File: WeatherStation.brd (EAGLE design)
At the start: 30.5 x 44.5 mm, 11 parts, among them J1 EDISON_CONNECTOR_FULLMOUNTING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, J2 EDISON_CONNECTOR_FULLHEADER

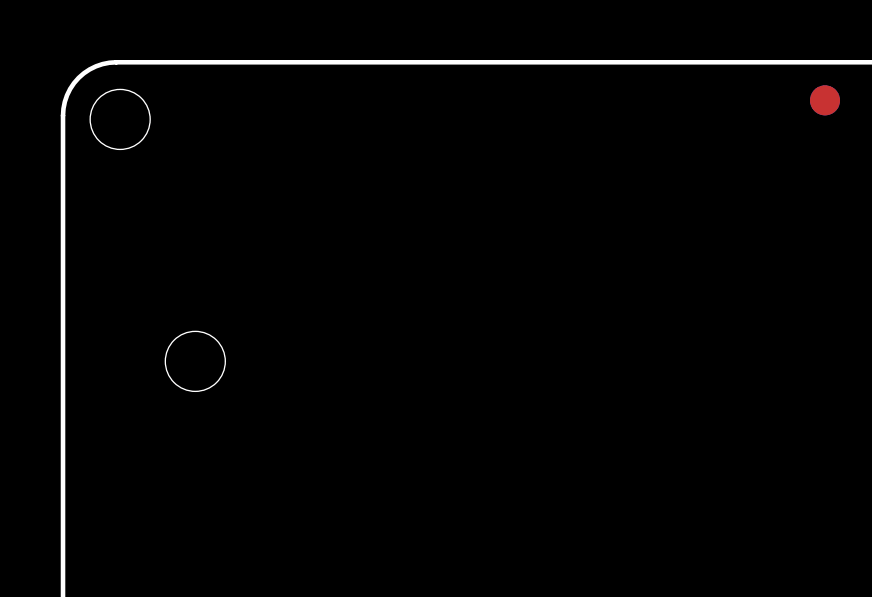
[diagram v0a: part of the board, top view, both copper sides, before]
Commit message: added MCP73831 circuit
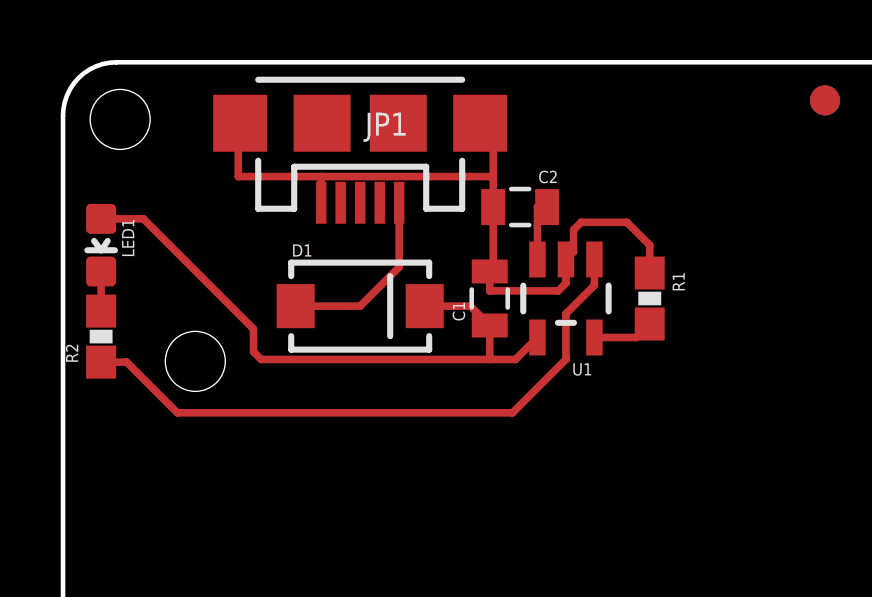
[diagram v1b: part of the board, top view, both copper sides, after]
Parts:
- added C1, C2: 4.7µF, SparkFun-Capacitors:0805
- added D1: MBRA140, SparkFun-DiscreteSemi:SMA-DIODE
- added JP1: USB-MICROB, SparkFun-Connectors:USB-MICROB
- added LED1: (no value), SparkFun-LED:LED-0603
- added R1: 2kΩ, SparkFun-Resistors:0603-RES
- added R2: 330Ω, SparkFun-Resistors:0603-RES
- added U1: MCP73831, SparkFun-PowerIC:SOT23-5
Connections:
- new net N$1: D1.A, JP1.VBUS
- new net N$2: C1.1, D1.C, LED1.A, U1.4
- new net N$4: LED1.C, R2.2
- new net N$5: R2.1, U1.1
- new net N$6: R1.2, U1.5
- new net VBAT: C2.1, U1.3
- net GND: now also C1.2, C2.2, JP1.GND, JP1.MT1, JP1.MT2, R1.1, U1.2
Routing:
- net GND: track 0.01 -> 25.7 mm
- net N$2: track 0.00 -> 20.8 mm
- net N$5: track 0.00 -> 20.7 mm
- net N$1: track 0.00 -> 6.13 mm
- net VBAT: track 0.00 -> 2.07 mm
- net N$6: track 0.00 -> 2.03 mm
- net N$4: track 0.00 -> 1.32 mm
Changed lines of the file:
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@@
 <?xml version="1.0" encoding="utf-8"?>
 <!DOCTYPE eagle SYSTEM "eagle.dtd">
-<eagle version="6.5.0">
+<eagle version="7.1.0">
 <drawing>
 <settings>
@@
 <pass name="Default">
 <param name="RoutingGrid" value="50mil"/>
+<param name="AutoGrid" value="1"/>
+<param name="Efforts" value="0"/>
+<param name="TopRouterVariant" value="1"/>
 <param name="tpViaShape" value="round"/>
 <param name="PrefDir.1" value="|"/>
@@
 <element name="FID3" library="SparkFun-Aesthetics" package="FIDUCIAL-1X2" value="FIDUCIAL1X2" x="1.27" y="5.08" locked="yes" rot="MR0"/>
 <element name="FID4" library="SparkFun-Aesthetics" package="FIDUCIAL-1X2" value="FIDUCIAL1X2" x="25.4" y="43.18" locked="yes" rot="MR0"/>
+<element name="JP1" library="SparkFun-Connectors" package="USB-MICROB" value="USB-MICROB" x="9.906" y="42.418" rot="R180">
+<attribute name="PROD_ID" value="CONN-09505" x="9.906" y="42.418" size="1.778" layer="27" rot="R180" display="off"/>
+</element>
+<element name="D1" library="SparkFun-DiscreteSemi" package="SMA-DIODE" value="MBRA140" x="9.906" y="36.322">
+<attribute name="PROD_ID" value="DIO-08053" x="9.906" y="36.322" size="1.778" layer="27" display="off"/>
+</element>
+<element name="U1" library="SparkFun-PowerIC" package="SOT23-5" value="MCP73831" x="16.764" y="36.576" smashed="yes" rot="R180">
+<attribute name="PROD_ID" value="IC-09995" x="16.764" y="36.576" size="1.778" layer="27" rot="R180" display="off"/>
+<attribute name="NAME" x="17.653" y="34.417" size="0.4064" layer="25" rot="R180"/>
+<attribute name="VALUE" x="16.7005" y="36.5125" size="0.3048" layer="27" rot="R180" align="center"/>
+</element>
+<element name="C1" library="SparkFun-Capacitors" package="0805" value="4.7µF" x="14.224" y="36.576" smashed="yes" rot="R90">
+<attribute name="NAME" x="13.3985" y="35.814" size="0.4064" layer="25" rot="R90"/>
+</element>
+<element name="R1" library="SparkFun-Resistors" package="0603-RES" value="2kΩ" x="19.558" y="36.576" rot="R270"/>
+<element name="C2" library="SparkFun-Capacitors" package="0805" value="4.7µF" x="15.24" y="39.624" smashed="yes" rot="R180">
+<attribute name="NAME" x="16.51" y="40.8305" size="0.4064" layer="25" rot="R180"/>
+</element>
+<element name="LED1" library="SparkFun-LED" package="LED-0603" value="" x="1.27" y="38.354" rot="R180"/>
+<element name="R2" library="SparkFun-Resistors" package="0603-RES" value="330Ω" x="1.27" y="35.306" rot="R90"/>
 </elements>
 <signals>
@@
 <wire x1="26.9438" y1="22.1798" x2="26.9494" y2="22.1742" width="0.1524" layer="1"/>
 <via x="27.1272" y="20.5232" extent="1-16" drill="0.3302"/>
+<contactref element="C1" pad="2"/>
+<contactref element="JP1" pad="MT2"/>
+<contactref element="JP1" pad="GND"/>
+<contactref element="JP1" pad="MT1"/>
+<contactref element="C2" pad="2"/>
+<contactref element="R1" pad="1"/>
+<contactref element="U1" pad="2"/>
+<wire x1="14.34" y1="39.624" x2="14.34" y2="40.64" width="0.254" layer="1"/>
+<wire x1="14.34" y1="40.64" x2="14.34" y2="42.418" width="0.254" layer="1"/>
+<wire x1="14.34" y1="42.418" x2="13.906" y2="42.418" width="0.254" layer="1"/>
+<wire x1="8.606" y1="39.768" x2="8.606" y2="40.64" width="0.254" layer="1"/>
+<wire x1="8.606" y1="40.64" x2="14.34" y2="40.64" width="0.254" layer="1"/>
+<wire x1="8.606" y1="40.64" x2="5.842" y2="40.64" width="0.254" layer="1"/>
+<wire x1="5.842" y1="40.64" x2="5.842" y2="42.418" width="0.254" layer="1"/>
+<wire x1="5.842" y1="42.418" x2="5.906" y2="42.418" width="0.254" layer="1"/>
+<wire x1="14.224" y1="37.476" x2="14.34" y2="37.592" width="0.254" layer="1"/>
+<wire x1="14.34" y1="37.592" x2="14.34" y2="39.624" width="0.254" layer="1"/>
+<wire x1="16.764" y1="37.8761" x2="16.764" y2="37.084" width="0.254" layer="1"/>
+<wire x1="16.764" y1="37.084" x2="16.51" y2="36.83" width="0.254" layer="1"/>
+<wire x1="16.51" y1="36.83" x2="14.224" y2="36.83" width="0.254" layer="1"/>
+<wire x1="14.224" y1="36.83" x2="14.224" y2="37.476" width="0.254" layer="1"/>
+<wire x1="19.558" y1="37.426" x2="19.558" y2="38.354" width="0.254" layer="1"/>
+<wire x1="19.558" y1="38.354" x2="18.796" y2="39.116" width="0.254" layer="1"/>
+<wire x1="18.796" y1="39.116" x2="17.272" y2="39.116" width="0.254" layer="1"/>
+<wire x1="17.272" y1="39.116" x2="17.018" y2="38.862" width="0.254" layer="1"/>
+<wire x1="17.018" y1="38.862" x2="17.018" y2="38.1301" width="0.254" layer="1"/>
+<wire x1="17.018" y1="38.1301" x2="16.764" y2="37.8761" width="0.254" layer="1"/>
+<wire x1="26.9438" y1="22.1798" x2="28.2448" y2="22.1742" width="0" layer="19" extent="1-1"/>
+<wire x1="25.96" y1="22.18" x2="26.9438" y2="22.1798" width="0" layer="19" extent="1-16"/>
+<wire x1="25.96" y1="22.1798" x2="25.96" y2="22.18" width="0" layer="19" extent="1-16"/>
+<wire x1="25.96" y1="22.98" x2="25.96" y2="22.18" width="0" layer="19" extent="16-16"/>
+<wire x1="25.96" y1="22.9798" x2="25.96" y2="22.98" width="0" layer="19" extent="1-16"/>
+<wire x1="25.96" y1="21.38" x2="25.96" y2="22.18" width="0" layer="19" extent="16-16"/>
+<wire x1="25.96" y1="21.3798" x2="25.96" y2="21.38" width="0" layer="19" extent="1-16"/>
+<wire x1="25.96" y1="20.98" x2="25.96" y2="21.38" width="0" layer="19" extent="16-16"/>
+<wire x1="25.96" y1="20.9798" x2="25.96" y2="20.98" width="0" layer="19" extent="1-16"/>
+<wire x1="25.96" y1="20.58" x2="25.96" y2="20.98" width="0" layer="19" extent="16-16"/>
+<wire x1="25.96" y1="20.5798" x2="25.96" y2="20.58" width="0" layer="19" extent="1-16"/>
+<wire x1="25.96" y1="20.18" x2="25.96" y2="20.58" width="0" layer="19" extent="16-16"/>
+<wire x1="25.96" y1="20.1798" x2="25.96" y2="20.18" width="0" layer="19" extent="1-16"/>
+<wire x1="27.1272" y1="20.5232" x2="25.96" y2="20.58" width="0" layer="19" extent="16-16"/>
+<wire x1="19.558" y1="37.426" x2="25.96" y2="22.98" width="0" layer="19" extent="1-16"/>
 </signal>
 <signal name="VSYS">
@@
 <wire x1="21.7988" y1="20.58" x2="21.799" y2="20.5798" width="0.1524" layer="1"/>
 </signal>
+<signal name="N$1">
+<contactref element="JP1" pad="VBUS"/>
+<contactref element="D1" pad="A"/>
+<wire x1="11.206" y1="39.768" x2="11.206" y2="37.622" width="0.254" layer="1"/>
+<wire x1="11.206" y1="37.622" x2="9.906" y2="36.322" width="0.254" layer="1"/>
+<wire x1="9.906" y1="36.322" x2="7.756" y2="36.322" width="0.254" layer="1"/>
+</signal>
+<signal name="N$2">
+<contactref element="D1" pad="C"/>
+<contactref element="U1" pad="4"/>
+<contactref element="C1" pad="1"/>
+<contactref element="LED1" pad="A"/>
+<wire x1="12.056" y1="36.322" x2="13.578" y2="36.322" width="0.254" layer="1"/>
+<wire x1="13.578" y1="36.322" x2="14.224" y2="35.676" width="0.254" layer="1"/>
+<wire x1="1.27" y1="39.231" x2="2.679" y2="39.231" width="0.254" layer="1"/>
+<wire x1="2.679" y1="39.231" x2="6.35" y2="35.56" width="0.254" layer="1"/>
+<wire x1="6.35" y1="35.56" x2="6.35" y2="34.798" width="0.254" layer="1"/>
+<wire x1="6.35" y1="34.798" x2="6.604" y2="34.544" width="0.254" layer="1"/>
+<wire x1="6.604" y1="34.544" x2="14.224" y2="34.544" width="0.254" layer="1"/>
+<wire x1="15.0821" y1="34.544" x2="15.814" y2="35.2759" width="0.254" layer="1"/>
+<wire x1="15.0821" y1="34.544" x2="14.224" y2="34.544" width="0.254" layer="1"/>
+<wire x1="14.224" y1="34.544" x2="14.224" y2="35.676" width="0.254" layer="1"/>
+</signal>
+<signal name="N$4">
+<contactref element="R2" pad="2"/>
+<contactref element="LED1" pad="C"/>
+<wire x1="1.27" y1="37.477" x2="1.27" y2="36.156" width="0.254" layer="1"/>
+</signal>
+<signal name="N$5">
+<contactref element="R2" pad="1"/>
+<contactref element="U1" pad="1"/>
+<wire x1="1.27" y1="34.456" x2="2.12" y2="34.456" width="0.254" layer="1"/>
+<wire x1="2.12" y1="34.456" x2="3.81" y2="32.766" width="0.254" layer="1"/>
+<wire x1="3.81" y1="32.766" x2="14.986" y2="32.766" width="0.254" layer="1"/>
+<wire x1="14.986" y1="32.766" x2="16.764" y2="34.544" width="0.254" layer="1"/>
+<wire x1="16.764" y1="34.544" x2="16.764" y2="36.068" width="0.254" layer="1"/>
+<wire x1="16.764" y1="36.068" x2="17.714" y2="37.018" width="0.254" layer="1"/>
+<wire x1="17.714" y1="37.018" x2="17.714" y2="37.8761" width="0.254" layer="1"/>
+</signal>
+<signal name="VBAT">
+<contactref element="U1" pad="3"/>
+<contactref element="C2" pad="1"/>
+<wire x1="15.814" y1="37.8761" x2="15.814" y2="39.624" width="0.254" layer="1"/>
+<wire x1="15.814" y1="39.624" x2="16.14" y2="39.624" width="0.254" layer="1"/>
+</signal>
+<signal name="N$6">
+<contactref element="R1" pad="2"/>
+<contactref element="U1" pad="5"/>
+<wire x1="17.714" y1="35.2759" x2="19.1079" y2="35.2759" width="0.254" layer="1"/>
+<wire x1="19.1079" y1="35.2759" x2="19.558" y2="35.726" width="0.254" layer="1"/>
+</signal>
 </signals>

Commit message: added 0.1" 2-pin battery header
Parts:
- added JP2: M02PTH, SparkFun-Connectors:1X02
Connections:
- net GND: now also JP2.1
- net VBAT: now also JP2.2
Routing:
- net VBAT: track 2.07 -> 7.01 mm
- net GND: track 25.7 -> 29.2 mm
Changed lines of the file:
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@@
 <element name="LED1" library="SparkFun-LED" package="LED-0603" value="" x="1.27" y="38.354" rot="R180"/>
 <element name="R2" library="SparkFun-Resistors" package="0603-RES" value="330Ω" x="1.27" y="35.306" rot="R90"/>
+<element name="JP2" library="SparkFun-Connectors" package="1X02" value="M02PTH" x="17.272" y="42.672" smashed="yes"/>
 </elements>
 <signals>
@@
 <wire x1="17.018" y1="38.862" x2="17.018" y2="38.1301" width="0.254" layer="1"/>
 <wire x1="17.018" y1="38.1301" x2="16.764" y2="37.8761" width="0.254" layer="1"/>
+<contactref element="JP2" pad="1"/>
+<wire x1="17.272" y1="42.672" x2="17.018" y2="42.418" width="0.254" layer="1"/>
+<wire x1="17.018" y1="42.418" x2="13.906" y2="42.418" width="0.254" layer="1"/>
 <wire x1="26.9438" y1="22.1798" x2="28.2448" y2="22.1742" width="0" layer="19" extent="1-1"/>
 <wire x1="25.96" y1="22.18" x2="26.9438" y2="22.1798" width="0" layer="19" extent="1-16"/>
@@
 <wire x1="15.814" y1="37.8761" x2="15.814" y2="39.624" width="0.254" layer="1"/>
 <wire x1="15.814" y1="39.624" x2="16.14" y2="39.624" width="0.254" layer="1"/>
+<contactref element="JP2" pad="2"/>
+<wire x1="19.812" y1="42.672" x2="16.764" y2="39.624" width="0.254" layer="1"/>
+<wire x1="16.764" y1="39.624" x2="16.14" y2="39.624" width="0.254" layer="1"/>
 </signal>
 <signal name="N$6">
